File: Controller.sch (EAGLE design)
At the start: 12 parts, among them IC1 TB6612FNG

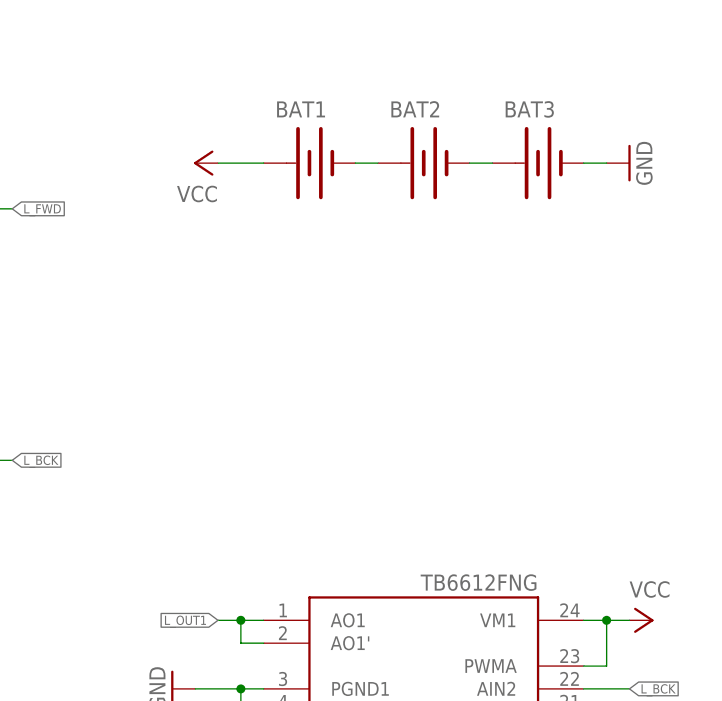
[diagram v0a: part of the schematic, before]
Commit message: add motor pads
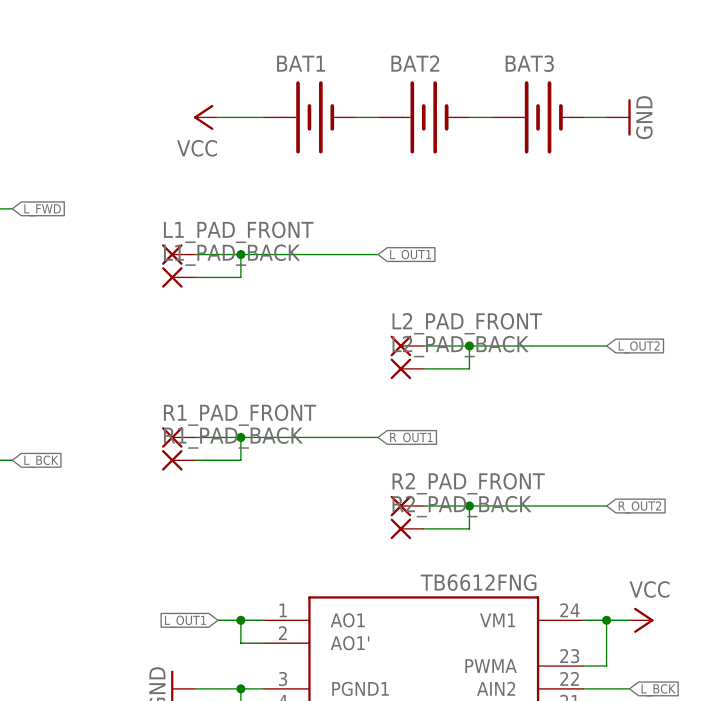
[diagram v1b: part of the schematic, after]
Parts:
- added L1_PAD_BACK, L1_PAD_FRONT, L2_PAD_BACK, L2_PAD_FRONT, R1_PAD_BACK, R1_PAD_FRONT, R2_PAD_BACK, R2_PAD_FRONT: WIREPADSMD5-2,5, wirepad:WIREPADSMD5-2,5
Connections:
- net L_OUT1: now also L1_PAD_BACK.P, L1_PAD_FRONT.P
- net L_OUT2: now also L2_PAD_BACK.P, L2_PAD_FRONT.P
- net R_OUT1: now also R1_PAD_BACK.P, R1_PAD_FRONT.P
- net R_OUT2: now also R2_PAD_BACK.P, R2_PAD_FRONT.P
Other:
- moved on the sheet: BAT1, BAT2, BAT3
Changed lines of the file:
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@@
 <part name="GND7" library="supply1" deviceset="GND" device=""/>
 <part name="GND8" library="supply1" deviceset="GND" device=""/>
+<part name="R2_PAD_FRONT" library="wirepad" deviceset="WIREPAD" device="SMD5-2,5"/>
+<part name="R1_PAD_FRONT" library="wirepad" deviceset="WIREPAD" device="SMD5-2,5"/>
+<part name="L2_PAD_FRONT" library="wirepad" deviceset="WIREPAD" device="SMD5-2,5"/>
+<part name="L1_PAD_FRONT" library="wirepad" deviceset="WIREPAD" device="SMD5-2,5"/>
+<part name="L1_PAD_BACK" library="wirepad" deviceset="WIREPAD" device="SMD5-2,5"/>
+<part name="L2_PAD_BACK" library="wirepad" deviceset="WIREPAD" device="SMD5-2,5"/>
+<part name="R1_PAD_BACK" library="wirepad" deviceset="WIREPAD" device="SMD5-2,5"/>
+<part name="R2_PAD_BACK" library="wirepad" deviceset="WIREPAD" device="SMD5-2,5"/>
 </parts>
 <sheets>
@@
 </plain>
 <instances>
-<instance part="BAT1" gate="G$1" x="73.66" y="101.6"/>
-<instance part="BAT2" gate="G$1" x="86.36" y="101.6"/>
-<instance part="BAT3" gate="G$1" x="99.06" y="101.6"/>
-<instance part="GND1" gate="1" x="109.22" y="101.6" rot="R90"/>
-<instance part="P+1" gate="VCC" x="60.96" y="101.6" rot="R90"/>
+<instance part="BAT1" gate="G$1" x="73.66" y="106.68"/>
+<instance part="BAT2" gate="G$1" x="86.36" y="106.68"/>
+<instance part="BAT3" gate="G$1" x="99.06" y="106.68"/>
+<instance part="GND1" gate="1" x="109.22" y="106.68" rot="R90"/>
+<instance part="P+1" gate="VCC" x="60.96" y="106.68" rot="R90"/>
 <instance part="L_FWD_BTN" gate="1" x="22.86" y="99.06" smashed="yes" rot="R270">
 <attribute name="NAME" x="15.24" y="105.41" size="1.778" layer="95"/>
@@
 <instance part="GND7" gate="1" x="58.42" y="20.32" rot="R270"/>
 <instance part="GND8" gate="1" x="58.42" y="43.18" rot="R270"/>
+<instance part="R2_PAD_FRONT" gate="G$1" x="83.82" y="63.5" smashed="yes">
+<attribute name="NAME" x="82.677" y="65.3542" size="1.778" layer="95"/>
+</instance>
+<instance part="R1_PAD_FRONT" gate="G$1" x="58.42" y="71.12" smashed="yes">
+<attribute name="NAME" x="57.277" y="72.9742" size="1.778" layer="95"/>
+</instance>
+<instance part="L2_PAD_FRONT" gate="G$1" x="83.82" y="81.28" smashed="yes">
+<attribute name="NAME" x="82.677" y="83.1342" size="1.778" layer="95"/>
+</instance>
+<instance part="L1_PAD_FRONT" gate="G$1" x="58.42" y="91.44" smashed="yes">
+<attribute name="NAME" x="57.277" y="93.2942" size="1.778" layer="95"/>
+</instance>
+<instance part="L1_PAD_BACK" gate="G$1" x="58.42" y="88.9" smashed="yes">
+<attribute name="NAME" x="57.277" y="90.7542" size="1.778" layer="95"/>
+</instance>
+<instance part="L2_PAD_BACK" gate="G$1" x="83.82" y="78.74" smashed="yes">
+<attribute name="NAME" x="82.677" y="80.5942" size="1.778" layer="95"/>
+</instance>
+<instance part="R1_PAD_BACK" gate="G$1" x="58.42" y="68.58" smashed="yes">
+<attribute name="NAME" x="57.277" y="70.4342" size="1.778" layer="95"/>
+</instance>
+<instance part="R2_PAD_BACK" gate="G$1" x="83.82" y="60.96" smashed="yes">
+<attribute name="NAME" x="82.677" y="62.8142" size="1.778" layer="95"/>
+</instance>
 </instances>
 <busses>
@@
 <pinref part="BAT1" gate="G$1" pin="-"/>
 <pinref part="BAT2" gate="G$1" pin="+"/>
-<wire x1="81.28" y1="101.6" x2="78.74" y2="101.6" width="0.1524" layer="91"/>
+<wire x1="81.28" y1="106.68" x2="78.74" y2="106.68" width="0.1524" layer="91"/>
 </segment>
 </net>
@@
 <pinref part="BAT2" gate="G$1" pin="-"/>
 <pinref part="BAT3" gate="G$1" pin="+"/>
-<wire x1="93.98" y1="101.6" x2="91.44" y2="101.6" width="0.1524" layer="91"/>
+<wire x1="93.98" y1="106.68" x2="91.44" y2="106.68" width="0.1524" layer="91"/>
 </segment>
 </net>
@@
 <segment>
 <pinref part="BAT1" gate="G$1" pin="+"/>
-<wire x1="63.5" y1="101.6" x2="68.58" y2="101.6" width="0.1524" layer="91"/>
+<wire x1="63.5" y1="106.68" x2="68.58" y2="106.68" width="0.1524" layer="91"/>
 <pinref part="P+1" gate="VCC" pin="VCC"/>
 </segment>
@@
 <segment>
 <pinref part="BAT3" gate="G$1" pin="-"/>
-<wire x1="104.14" y1="101.6" x2="106.68" y2="101.6" width="0.1524" layer="91"/>
+<wire x1="104.14" y1="106.68" x2="106.68" y2="106.68" width="0.1524" layer="91"/>
 <pinref part="GND1" gate="1" pin="GND"/>
 </segment>
@@
 <label x="63.5" y="50.8" size="1.016" layer="95" rot="R180" xref="yes"/>
 </segment>
+<segment>
+<pinref part="L1_PAD_BACK" gate="G$1" pin="P"/>
+<wire x1="60.96" y1="88.9" x2="66.04" y2="88.9" width="0.1524" layer="91"/>
+<wire x1="66.04" y1="88.9" x2="66.04" y2="91.44" width="0.1524" layer="91"/>
+<wire x1="66.04" y1="91.44" x2="81.28" y2="91.44" width="0.1524" layer="91"/>
+<pinref part="L1_PAD_FRONT" gate="G$1" pin="P"/>
+<wire x1="60.96" y1="91.44" x2="66.04" y2="91.44" width="0.1524" layer="91"/>
+<junction x="66.04" y="91.44"/>
+<label x="81.28" y="91.44" size="1.016" layer="95" xref="yes"/>
+</segment>
 </net>
 <net name="L_OUT2" class="0">
@@
 <label x="63.5" y="35.56" size="1.016" layer="95" rot="R180" xref="yes"/>
 </segment>
+<segment>
+<pinref part="L2_PAD_BACK" gate="G$1" pin="P"/>
+<wire x1="86.36" y1="78.74" x2="91.44" y2="78.74" width="0.1524" layer="91"/>
+<wire x1="91.44" y1="78.74" x2="91.44" y2="81.28" width="0.1524" layer="91"/>
+<pinref part="L2_PAD_FRONT" gate="G$1" pin="P"/>
+<wire x1="86.36" y1="81.28" x2="91.44" y2="81.28" width="0.1524" layer="91"/>
+<wire x1="91.44" y1="81.28" x2="106.68" y2="81.28" width="0.1524" layer="91"/>
+<junction x="91.44" y="81.28"/>
+<label x="106.68" y="81.28" size="1.016" layer="95" xref="yes"/>
+</segment>
 </net>
 <net name="R_OUT2" class="0">
@@
 <label x="63.5" y="27.94" size="1.016" layer="95" rot="R180" xref="yes"/>
 </segment>
+<segment>
+<pinref part="R2_PAD_BACK" gate="G$1" pin="P"/>
+<wire x1="86.36" y1="60.96" x2="91.44" y2="60.96" width="0.1524" layer="91"/>
+<wire x1="91.44" y1="60.96" x2="91.44" y2="63.5" width="0.1524" layer="91"/>
+<pinref part="R2_PAD_FRONT" gate="G$1" pin="P"/>
+<wire x1="91.44" y1="63.5" x2="86.36" y2="63.5" width="0.1524" layer="91"/>
+<wire x1="91.44" y1="63.5" x2="106.68" y2="63.5" width="0.1524" layer="91"/>
+<junction x="91.44" y="63.5"/>
+<label x="106.68" y="63.5" size="1.016" layer="95" xref="yes"/>
+</segment>
 </net>
 <net name="R_OUT1" class="0">
@@
 <label x="63.5" y="12.7" size="1.016" layer="95" rot="R180" xref="yes"/>
 </segment>
-</net>
+<segment>
+<pinref part="R1_PAD_BACK" gate="G$1" pin="P"/>
+<wire x1="60.96" y1="68.58" x2="66.04" y2="68.58" width="0.1524" layer="91"/>
+<wire x1="66.04" y1="68.58" x2="66.04" y2="71.12" width="0.1524" layer="91"/>
+<pinref part="R1_PAD_FRONT" gate="G$1" pin="P"/>
+<wire x1="66.04" y1="71.12" x2="60.96" y2="71.12" width="0.1524" layer="91"/>
+<wire x1="66.04" y1="71.12" x2="81.28" y2="71.12" width="0.1524" layer="91"/>
+<junction x="66.04" y="71.12"/>
+<label x="81.28" y="71.12" size="1.016" layer="95" xref="yes"/>
+</segment>
+</net>

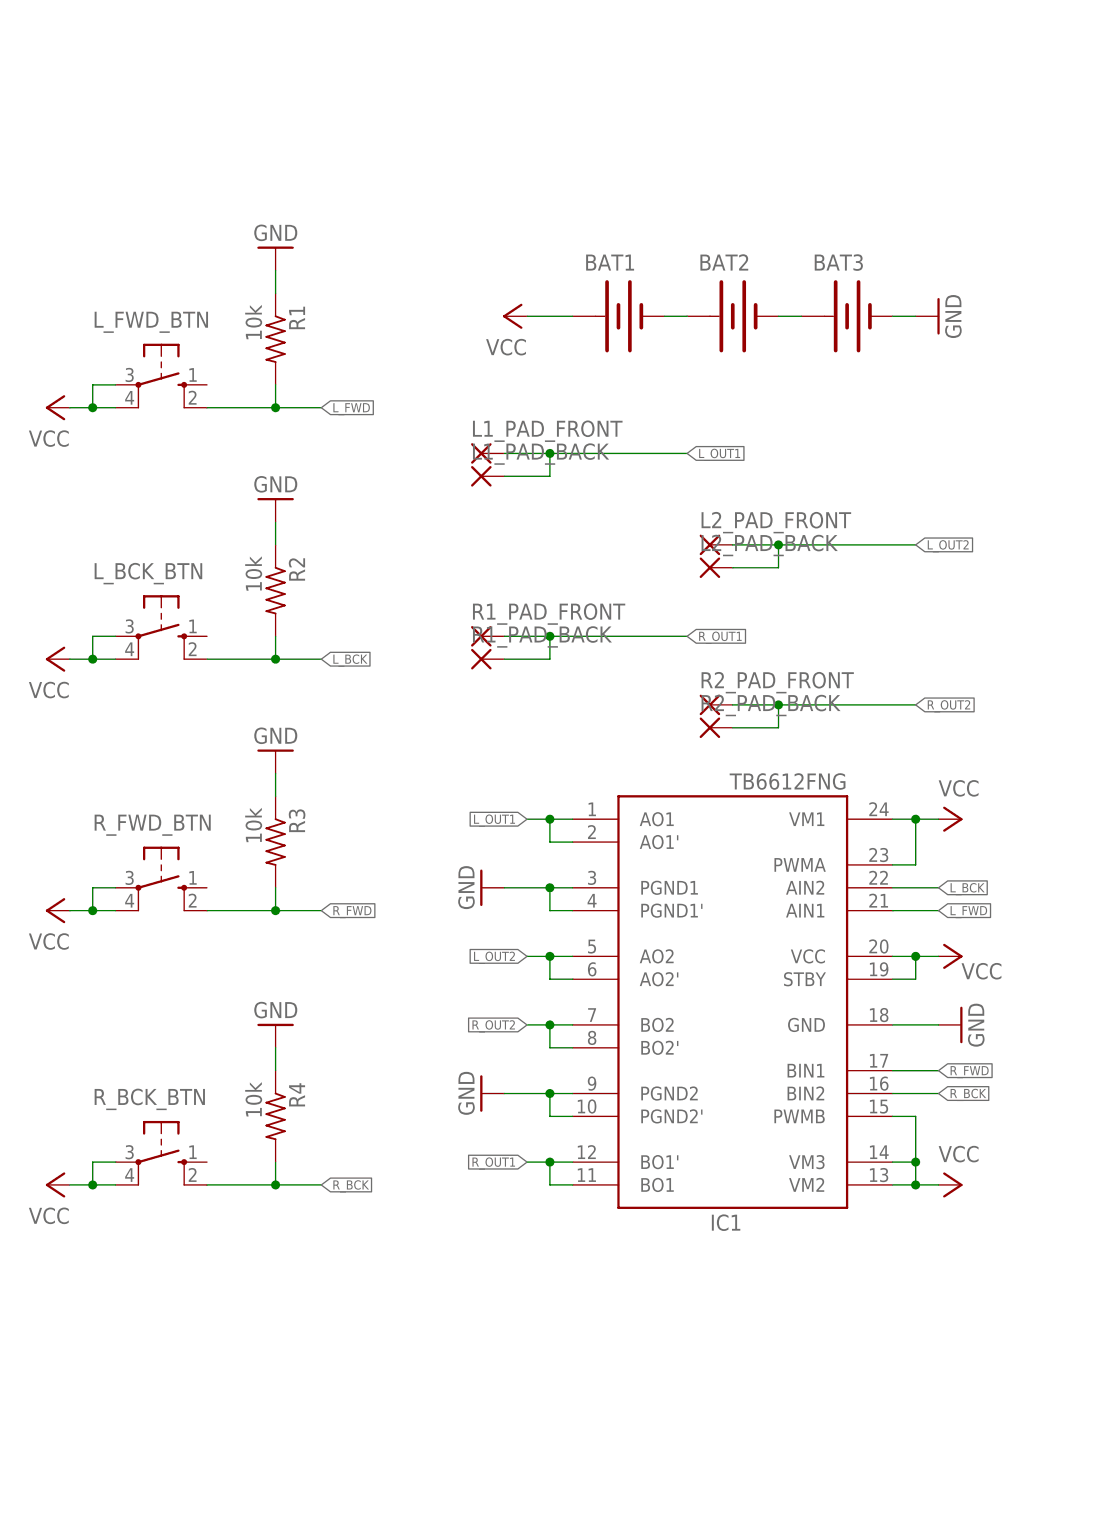
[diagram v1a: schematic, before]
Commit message: add fancy A5 portrait frame to schematic
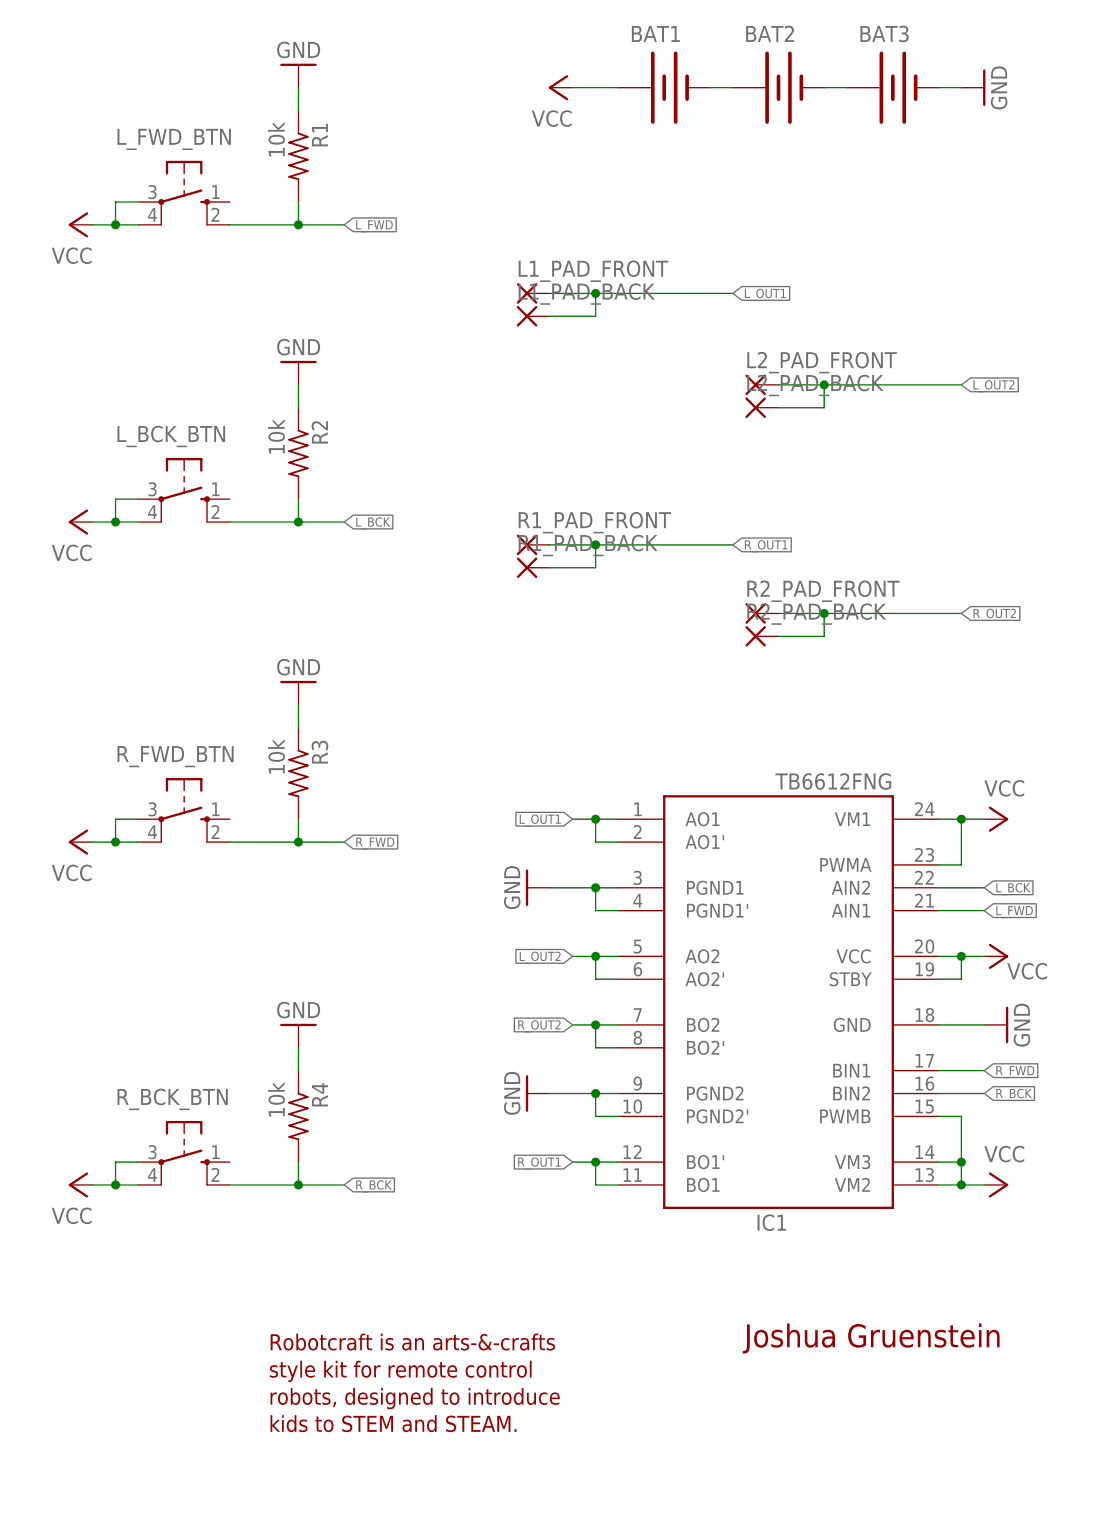
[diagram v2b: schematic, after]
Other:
- note added: "Joshua Gruenstein"
- note added: "Robotcraft is an arts-&-crafts style kit for remote control robots, designed to introduce kids to STEM and STEAM."
- moved on the sheet: BAT1, BAT2, BAT3, IC1, L1_PAD_BACK, L1_PAD_FRONT, L2_PAD_BACK, L2_PAD_FRONT, L_BCK_BTN, L_FWD_BTN, R1, R1_PAD_BACK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

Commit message: cosmetic PCB upgrades
added OSHW logo to bottom silkscreen
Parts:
- added GOLD_ORB_SM1: OSHWLOGO_GOLD_ORB_MED, bfl:OSHWLOGO_GOLD_ORB_MED
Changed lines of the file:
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@@
 <part name="R2_PAD_BACK" library="wirepad" deviceset="WIREPAD" device="SMD5-2,5"/>
 <part name="FRAME1" library="frames" deviceset="A5P-LOC" device=""/>
+<part name="GOLD_ORB_SM1" library="bfl" deviceset="OSHWLOGO" device="_GOLD_ORB_MED"/>
 </parts>
 <sheets>
@@
 </instance>
 <instance part="FRAME1" gate="G$1" x="0" y="-27.94"/>
+<instance part="GOLD_ORB_SM1" gate="G$1" x="20.32" y="-12.7"/>
 </instances>
 <busses>

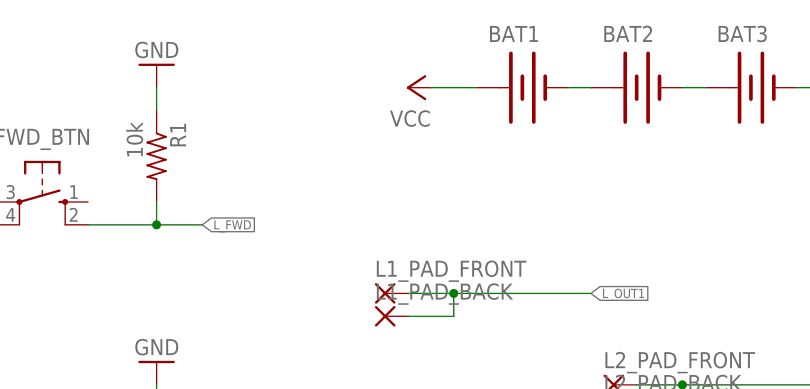
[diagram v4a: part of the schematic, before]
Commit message: add diode to board and schematic
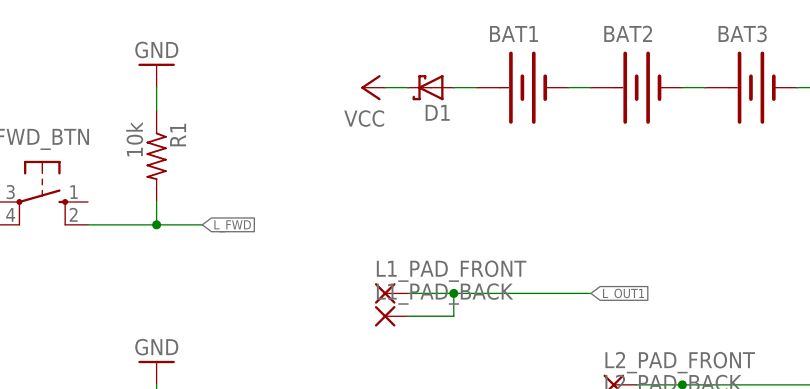
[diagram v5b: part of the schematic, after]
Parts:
- added D1: (no value), diode:SCHOTTKY-DIODESMC
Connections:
- new net N$3: BAT1.+, D1.A
- net VCC: now also D1.C; no longer BAT1.+
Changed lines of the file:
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@@
 <part name="FRAME1" library="frames" deviceset="A5P-LOC" device=""/>
 <part name="GOLD_ORB_SM1" library="bfl" deviceset="OSHWLOGO" device="_GOLD_ORB_MED"/>
+<part name="D1" library="diode" deviceset="SCHOTTKY-DIODE" device="SMC"/>
 </parts>
 <sheets>
@@
 <instance part="BAT3" gate="G$1" x="104.14" y="132.08"/>
 <instance part="GND1" gate="1" x="114.3" y="132.08" rot="R90"/>
-<instance part="P+1" gate="VCC" x="66.04" y="132.08" rot="R90"/>
+<instance part="P+1" gate="VCC" x="60.96" y="132.08" rot="R90"/>
 <instance part="L_FWD_BTN" gate="1" x="25.4" y="119.38" smashed="yes" rot="R270">
 <attribute name="NAME" x="17.78" y="125.73" size="1.778" layer="95"/>
@@
 <instance part="FRAME1" gate="G$1" x="0" y="-27.94"/>
 <instance part="GOLD_ORB_SM1" gate="G$1" x="20.32" y="-12.7"/>
+<instance part="D1" gate="G$1" x="68.58" y="132.08" rot="R180"/>
 </instances>
 <busses>
@@
 </net>
 <net name="VCC" class="0">
-<segment>
-<pinref part="BAT1" gate="G$1" pin="+"/>
-<wire x1="68.58" y1="132.08" x2="73.66" y2="132.08" width="0.1524" layer="91"/>
-<pinref part="P+1" gate="VCC" pin="VCC"/>
-</segment>
 <segment>
 <pinref part="L_FWD_BTN" gate="1" pin="P"/>
@@
 <junction x="111.76" y="12.7"/>
 </segment>
+<segment>
+<pinref part="P+1" gate="VCC" pin="VCC"/>
+<pinref part="D1" gate="G$1" pin="C"/>
+<wire x1="63.5" y1="132.08" x2="66.04" y2="132.08" width="0.1524" layer="91"/>
+</segment>
 </net>
 <net name="GND" class="0">
@@
 </segment>
 </net>
+<net name="N$3" class="0">
+<segment>
+<pinref part="D1" gate="G$1" pin="A"/>
+<pinref part="BAT1" gate="G$1" pin="+"/>
+<wire x1="71.12" y1="132.08" x2="73.66" y2="132.08" width="0.1524" layer="91"/>
+</segment>
+</net>
